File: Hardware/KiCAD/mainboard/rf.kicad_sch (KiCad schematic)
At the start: 41 parts, among them J1 Conn_Coaxial, U2 CC1200, Y3 40 MHz

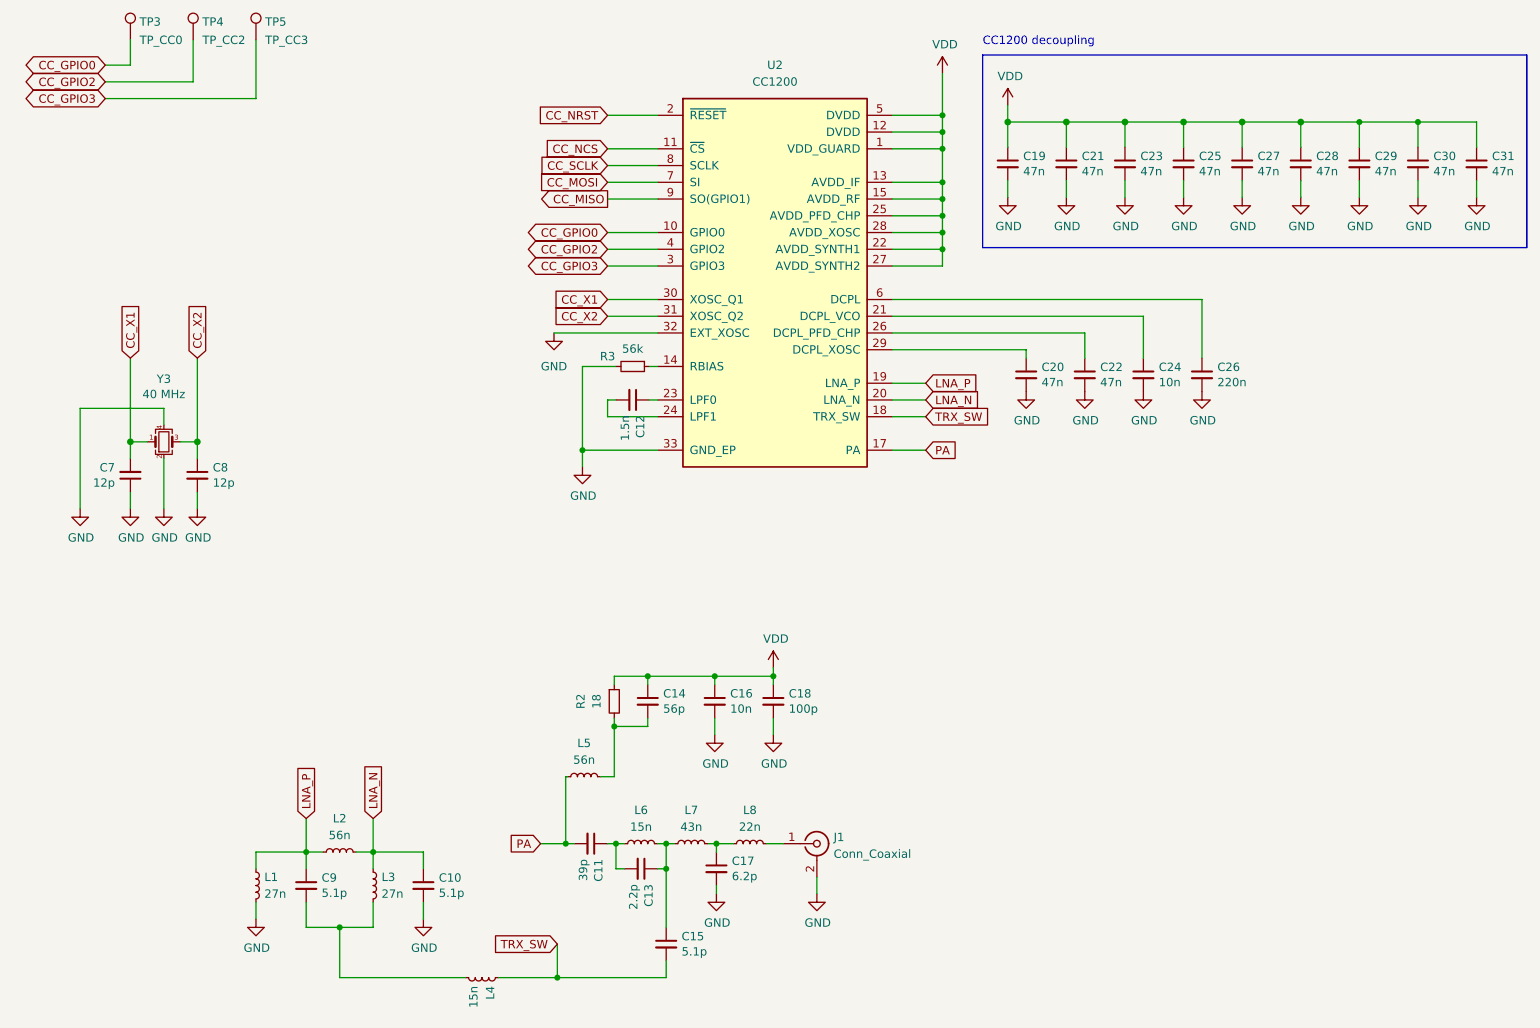
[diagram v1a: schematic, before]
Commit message: MCU swap
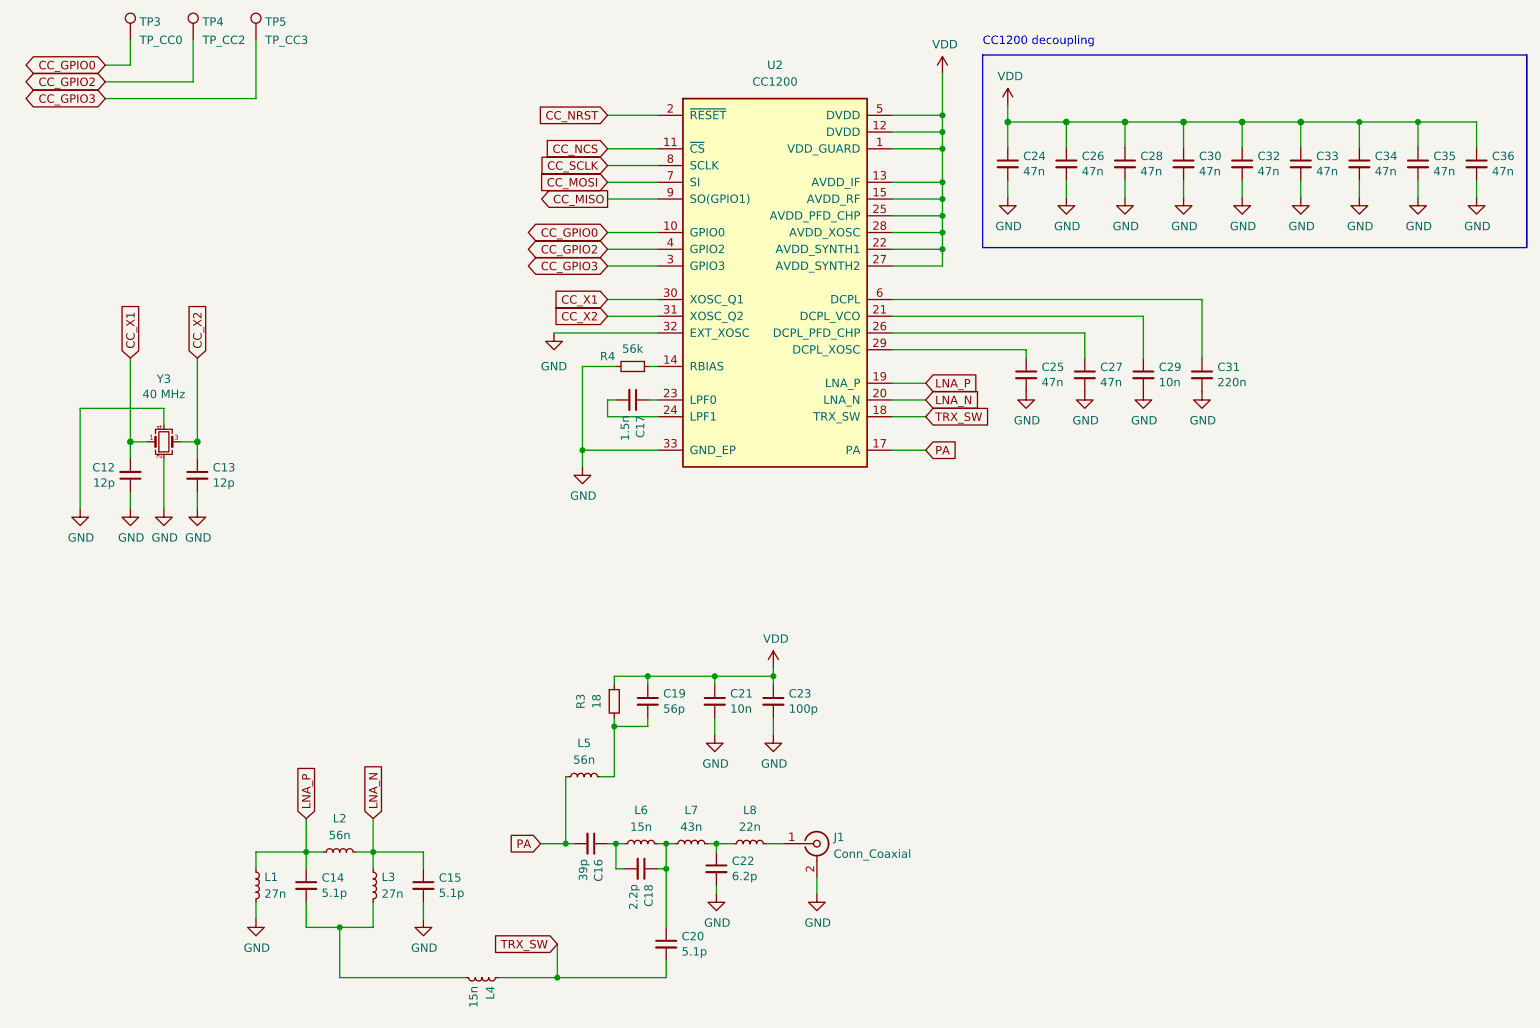
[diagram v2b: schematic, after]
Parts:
- renumbered C7 to C12, C8 to C13, C9 to C14, C10 to C15, C11 to C16, C12 to C17, C13 to C18, C14 to C19, C15 to C20, C16 to C21, C17 to C22, C18 to C23, C19 to C24, C20 to C25, C21 to C26, C22 to C27, C23 to C28, C24 to C29, C25 to C30, C26 to C31, C27 to C32, C28 to C33, C29 to C34, C30 to C35, C31 to C36, R2 to R3, R3 to R4

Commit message: Removed RTC
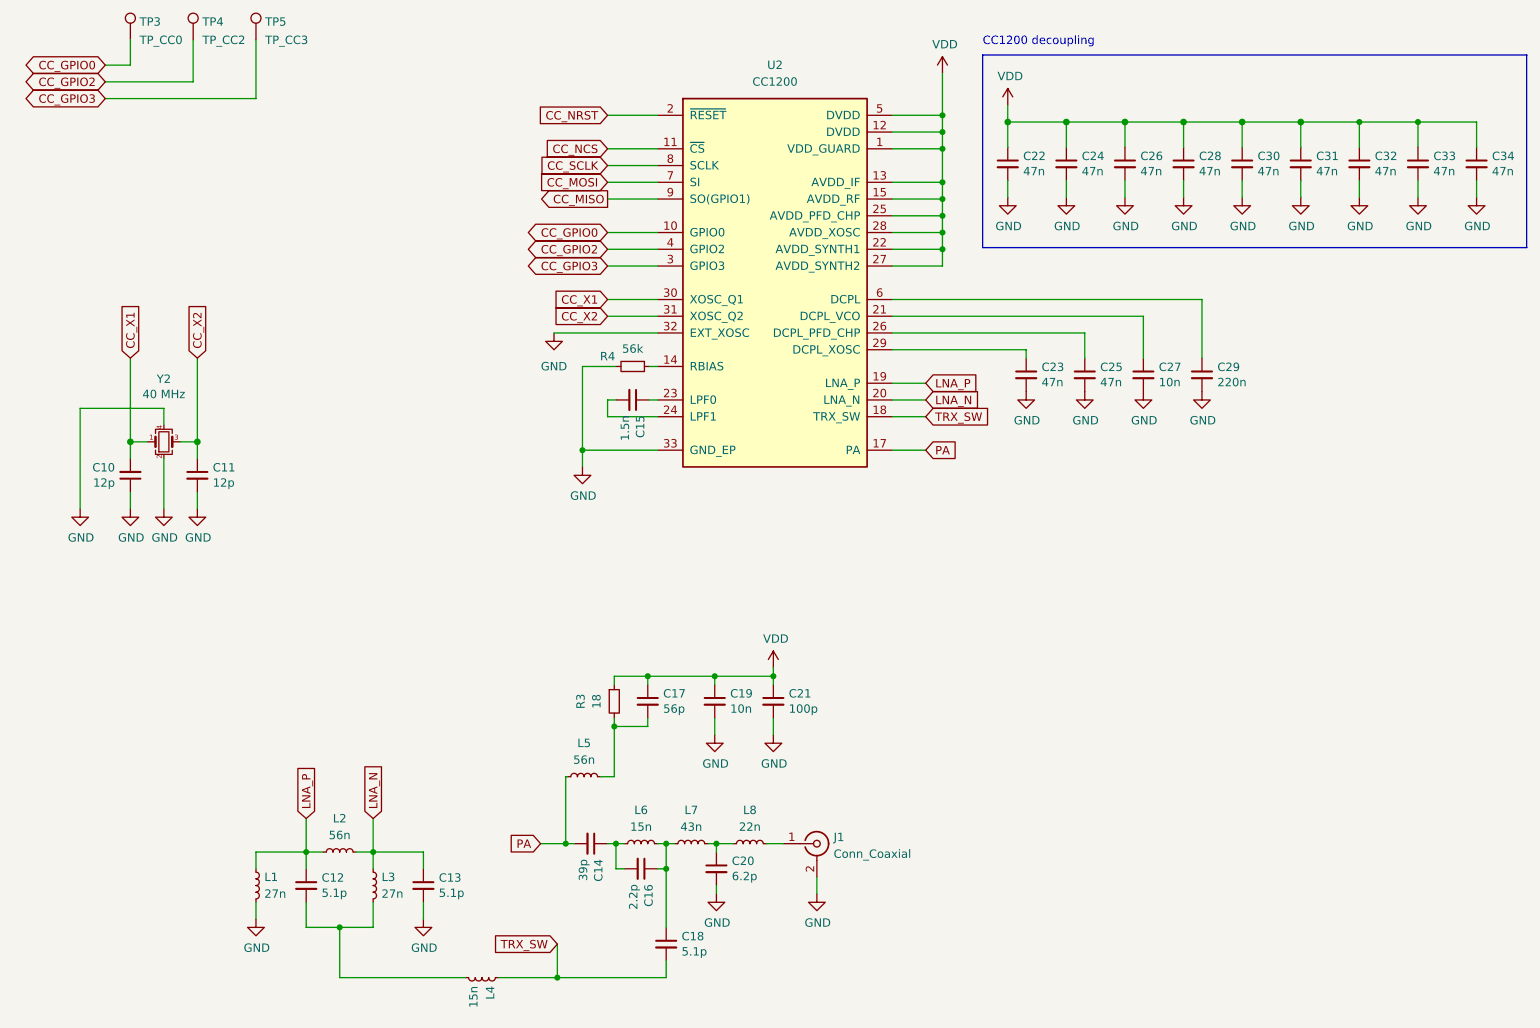
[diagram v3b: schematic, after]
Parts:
- renumbered C12 to C10, C13 to C11, C14 to C12, C15 to C13, C16 to C14, C17 to C15, C18 to C16, C19 to C17, C20 to C18, C21 to C19, C22 to C20, C23 to C21, C24 to C22, C25 to C23, C26 to C24, C27 to C25, C28 to C26, C29 to C27, C30 to C28, C31 to C29, C32 to C30, C33 to C31, C34 to C32, C35 to C33, C36 to C34, Y3 to Y2
